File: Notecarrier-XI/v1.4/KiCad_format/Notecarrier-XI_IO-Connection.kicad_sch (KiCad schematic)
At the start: 11 parts, among them J1 Header 2.54mm 1x4, J2 SM04B-SRSS-TB(LF)(SN), J3 S2B-PH-SM4-K-TB, J8 B2B-PH-SM4-TBT (LF)(SN), P1 Header 2.54mm 1x16, P2 Header 2.54mm 1x16, P4 12402012E212A

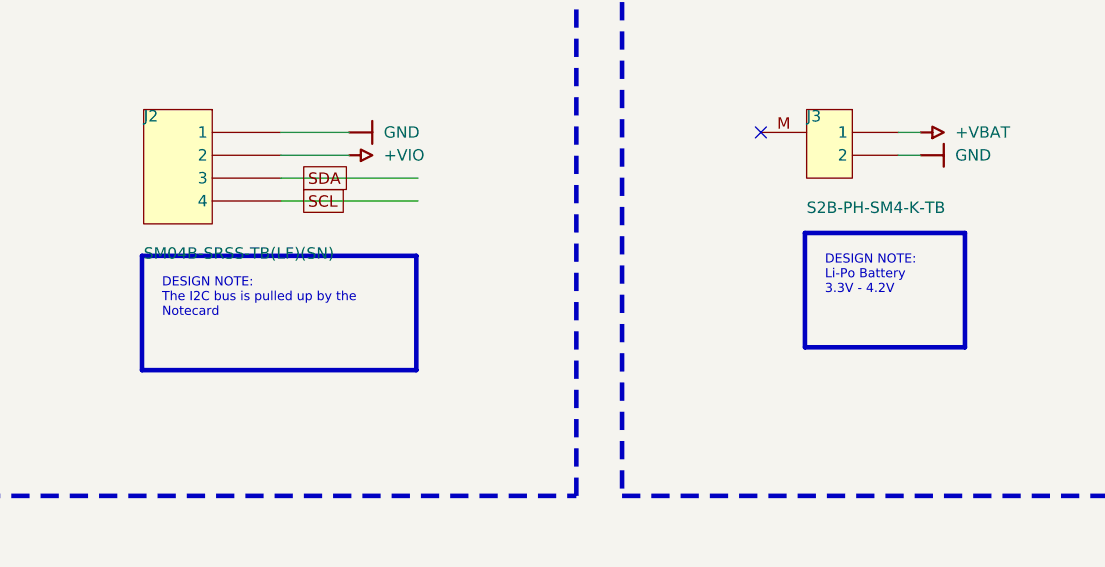
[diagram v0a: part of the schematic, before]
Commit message: Ports: convert design-note text_boxes to plain text so kicanvas can render them
kicanvas parses text_box but never paints it - true of the current upstream
build too, which is byte-identical to the one vendored here. On the published
datasheet pages that left the design notes (charger limits, regulator specs,
population notes) as empty frames, and on Cygnet, whose note frames ARE the
text_boxes, the notes were entirely invisible. KiCad renders plain text and
rectangles identically to what it drew before, and kicanvas renders both, so
the 28 text_boxes across 12 sheets on 6 boards become plain text items - plus a
synthesized rectangle carrying the exact stroke and fill for the 5 Cygnet notes
whose box itself is visible (yellow-filled with a border).

Two things made this more than a mechanical swap:

- text_box soft-wraps and plain text does not. A first attempt left two notes
  overflowing their frames and colliding with a neighbouring note. The wrap is
  now frozen at exactly the line breaks KiCad itself used: each sheet's
  before-conversion PDF carries a hidden searchable text layer, and the
  converter reads the wrapped lines out of the note's own rectangle, guarded by
  a word-for-word equality check against the source text. That guard earned its
  keep twice, catching part-number labels that physically overlap two of the
  note boxes.

- kicanvas draws default-colored text in its theme color, which is white - and
  two Cygnet notes sit on yellow fills. Those five framed notes now carry an
  explicit (0,0,193) font color, sampled from KiCad's own plot of the same
  notes, so KiCad's output is unchanged and kicanvas is readable.

Verified per board: netlists byte-equal before and after; KiCad PDF renders
differ only by sub-millimetre line pitch (0.05-0.7% of sampled pixels, every
note inside its frame - checked visually on the worst sheets); kicanvas renders
all 12 sheets with the notes now visible; committed screenshots regenerated,
all six boards PASS.

Co-Aut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
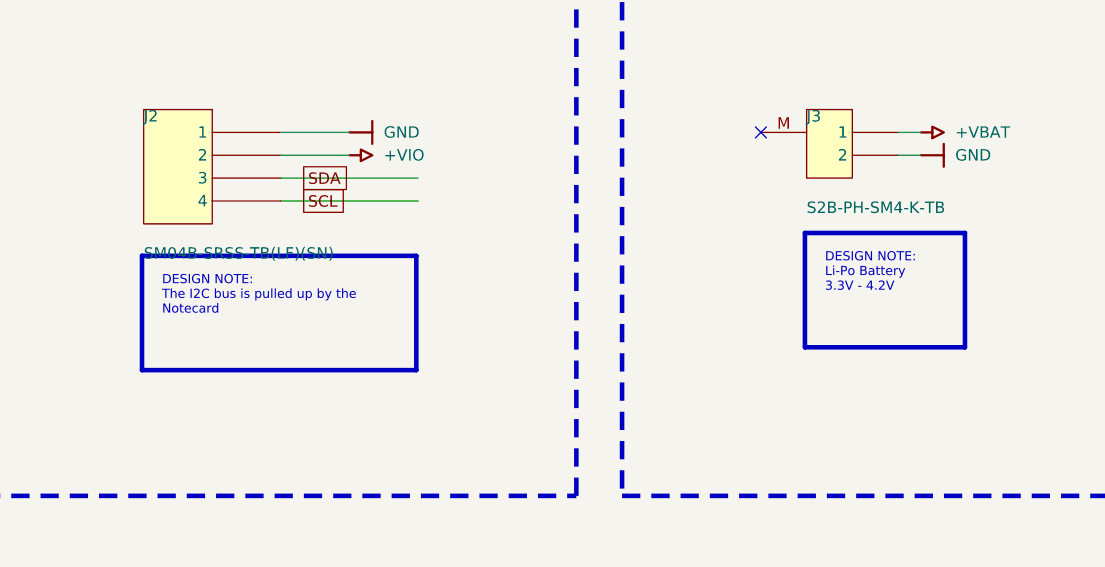
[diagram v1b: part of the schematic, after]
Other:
- note added: "DESIGN NOTE: Li-Po Battery 3.3V - 4.2V"
- note added: "DESIGN NOTE: The I2C bus is pulled up by the Notecard"
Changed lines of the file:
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@@
 		)
 	)
-	(text_box "DESIGN NOTE:\nThe I2C bus is pulled up by the Notecard\n"
+	(text "DESIGN NOTE:\nThe I2C bus is pulled up by the\nNotecard\n"
 		(exclude_from_sim no)
-		(at 247.464 179.9062 0)
-		(size -27.94 10.16)
-		(margins 0.9525 0.9525 0.9525 0.9525)
-		(stroke
-			(width -0.0001)
-			(type default)
-			(color 0 0 0 1)
-		)
-		(fill
-			(type none)
-		)
+		(at 220.476 180.859 0)
 		(effects
 			(font
@@
 		)
 	)
-	(text_box "DESIGN NOTE:\nLi-Po Battery\n3.3V - 4.2V"
+	(text "DESIGN NOTE:\nLi-Po Battery\n3.3V - 4.2V"
 		(exclude_from_sim no)
-		(at 312.234 177.3662 0)
-		(size -19.05 10.16)
-		(margins 0.9525 0.9525 0.9525 0.9525)
-		(stroke
-			(width -0.0001)
-			(type default)
-			(color 0 0 0 1)
-		)
-		(fill
-			(type none)
-		)
+		(at 294.136 178.319 0)
 		(effects
 			(font
